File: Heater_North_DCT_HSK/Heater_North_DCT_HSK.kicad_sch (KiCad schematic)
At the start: 3 parts, among them J1 North_Heater_1, J2 North_Heater_2, J3 Internal_Heater_DCT_HSK_Box

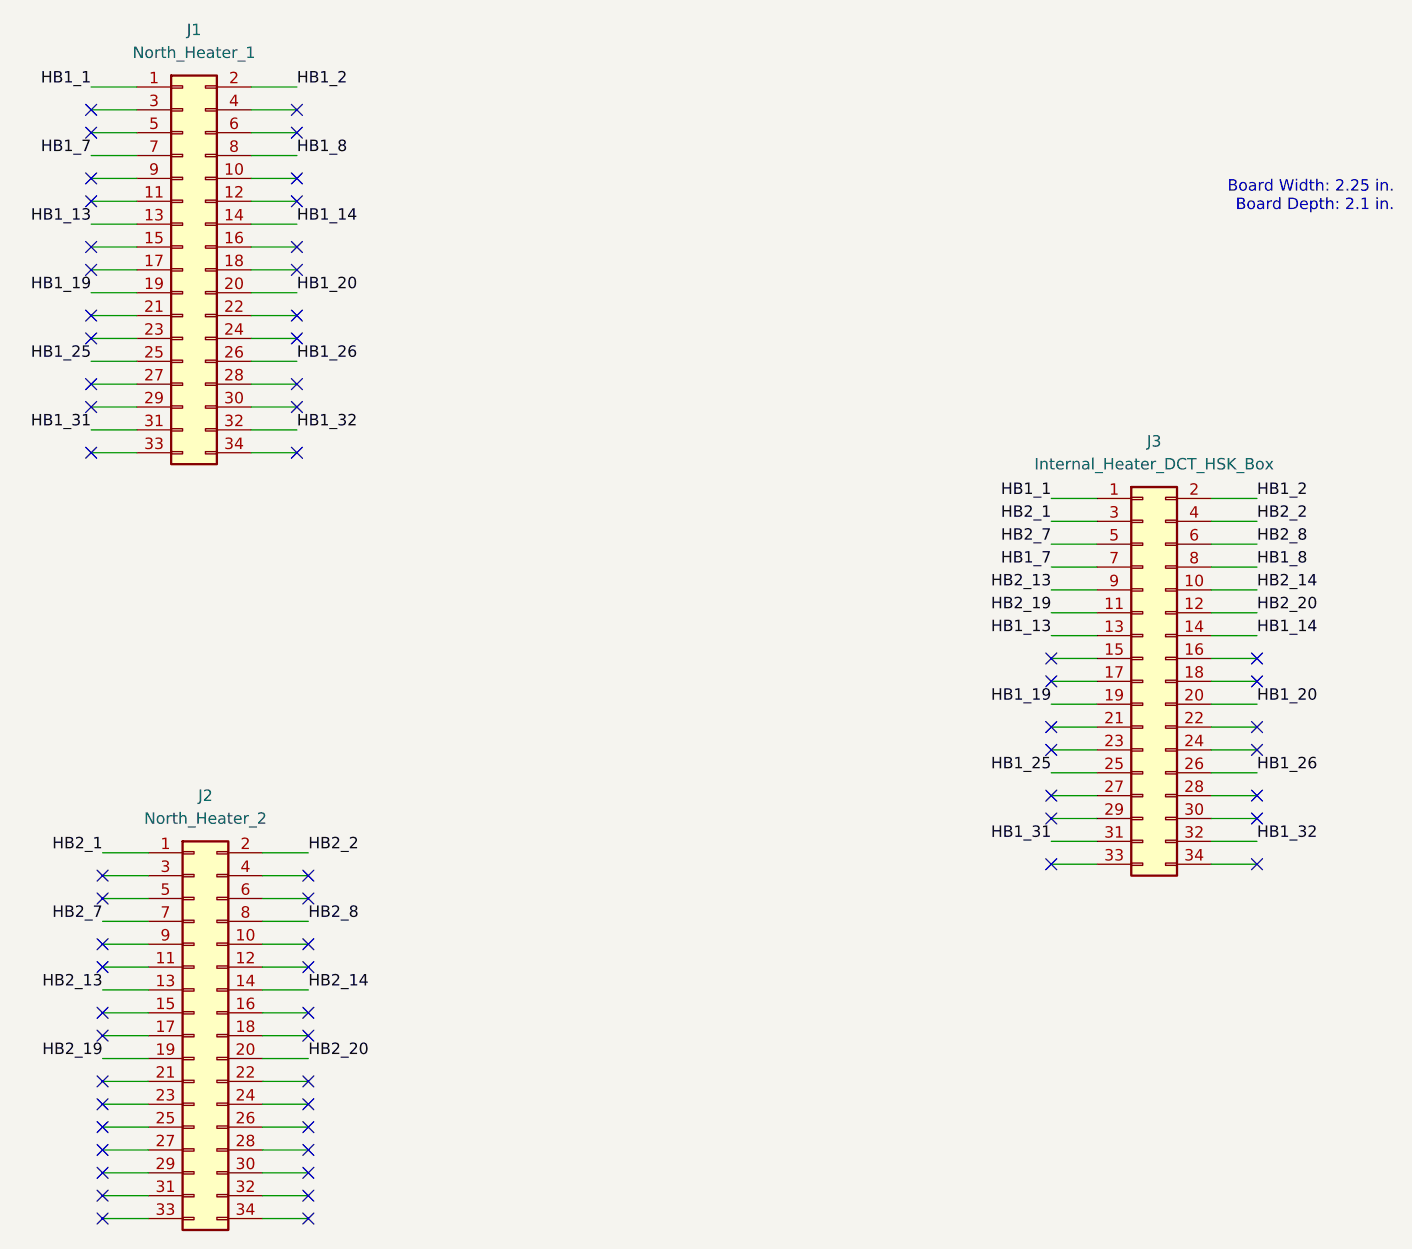
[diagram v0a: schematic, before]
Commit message: New feedthrough PCBs to access spare heater channels for flowcontroller heaters.
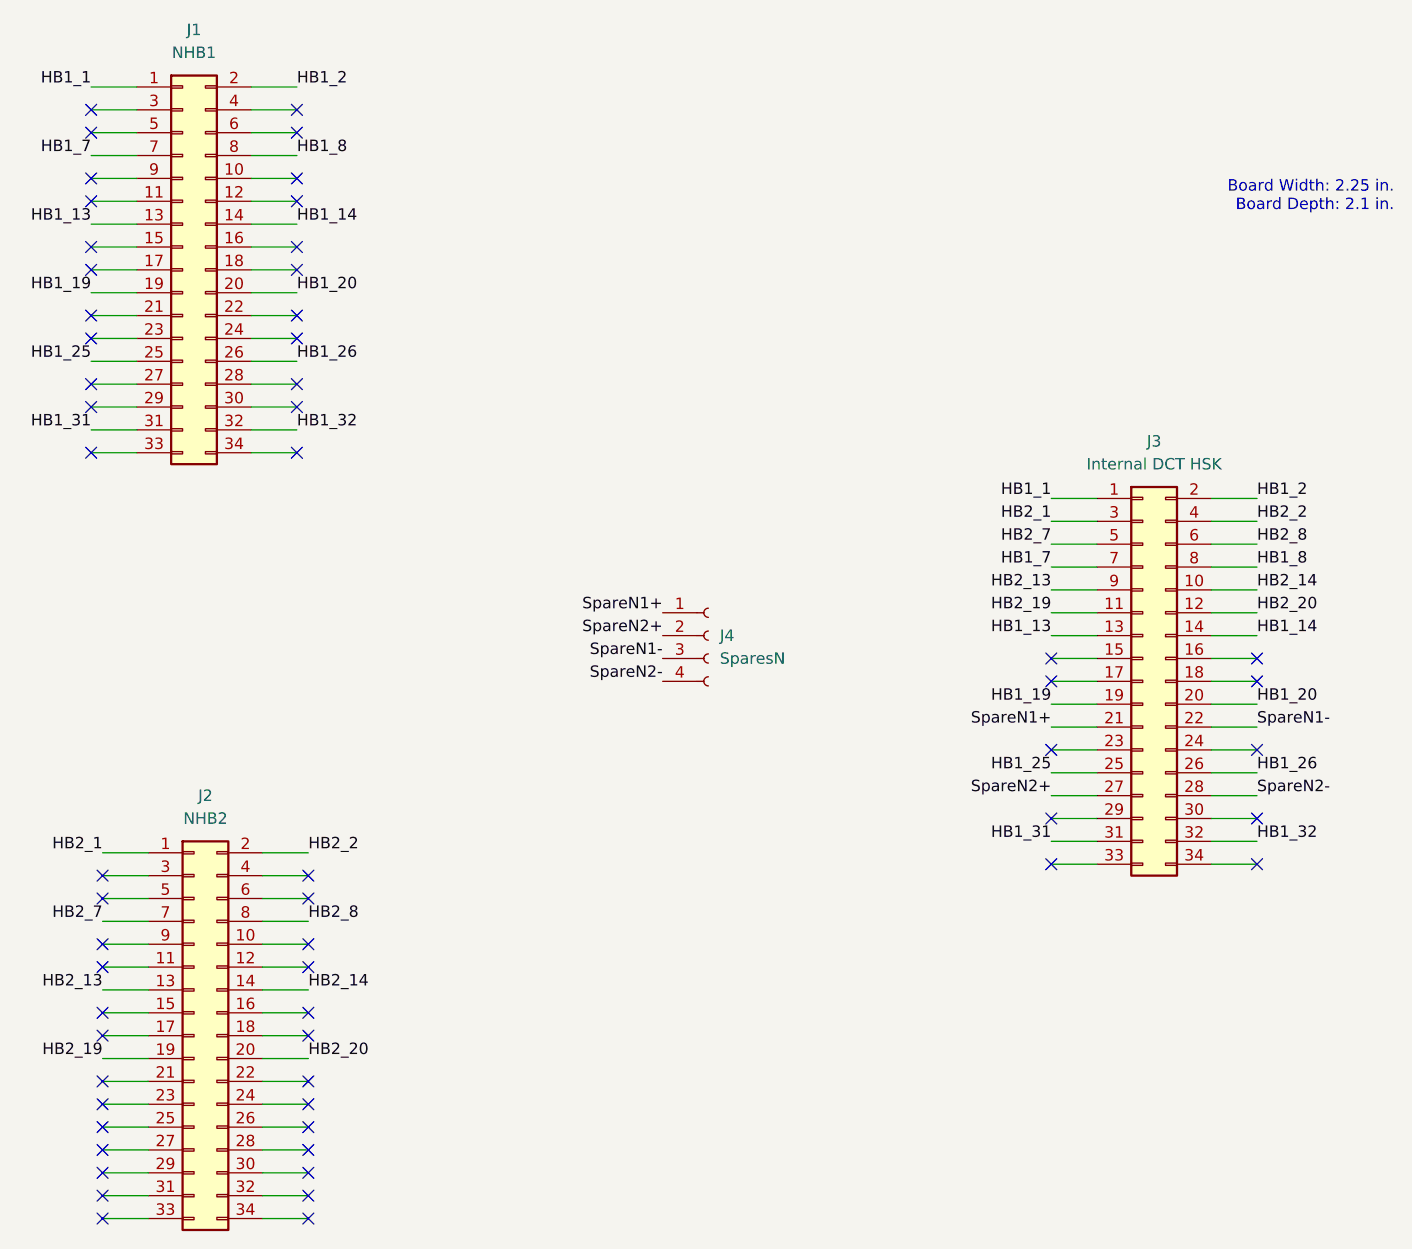
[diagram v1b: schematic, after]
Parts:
- added J4: SparesN, Connector_Molex:Molex_Micro-Fit_3.0_43045-0400_2x02_P3.00mm_Horizontal, symbol Connector:Conn_01x04_Socket
- J1: value North_Heater_1 -> NHB1
- J2: value North_Heater_2 -> NHB2
- J3: value Internal_Heater_DCT_HSK_Box -> Internal DCT HSK
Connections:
- net SpareN1+: now reaches J3.21 (Pin_21)
- net SpareN1+: now also J4.1 (Pin_1)
- net SpareN1-: now reaches J3.22 (Pin_22)
- net SpareN1-: now also J4.3 (Pin_3)
- net SpareN2+: now reaches J3.27 (Pin_27)
- net SpareN2+: now also J4.2 (Pin_2)
- net SpareN2-: now reaches J3.28 (Pin_28)
- net SpareN2-: now also J4.4 (Pin_4)
- no-connect marks 62 -> 58
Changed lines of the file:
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@@
   (no_connect (at 101.6 74.93))
   (no_connect (at 78.74 82.55))
-  (no_connect (at 208.28 120.65))
   (no_connect (at 185.42 123.19))
   (no_connect (at 78.74 62.23))
@@
   (no_connect (at 208.28 123.19))
   (no_connect (at 101.6 62.23))
-  (no_connect (at 208.28 113.03))
   (no_connect (at 101.6 59.69))
   (no_connect (at 102.87 167.64))
@@
   (no_connect (at 208.28 105.41))
   (no_connect (at 101.6 67.31))
-  (no_connect (at 185.42 120.65))
   (no_connect (at 78.74 59.69))
   (no_connect (at 101.6 69.85))
   (no_connect (at 78.74 74.93))
-  (no_connect (at 185.42 113.03))
   (no_connect (at 185.42 128.27))
   (no_connect (at 208.28 115.57))
@@
     (effects (font (size 1.27 1.27)) (justify left bottom))
   )
+  (label "SpareN1+" (at 142.24 100.33 180) (fields_autoplaced)
+    (effects (font (size 1.27 1.27)) (justify right bottom))
+  )
   (label "HB1_19" (at 185.42 110.49 180) (fields_autoplaced)
     (effects (font (size 1.27 1.27)) (justify right bottom))
   )
+  (label "SpareN2-" (at 142.24 107.95 180) (fields_autoplaced)
+    (effects (font (size 1.27 1.27)) (justify right bottom))
+  )
+  (label "SpareN2+" (at 142.24 102.87 180) (fields_autoplaced)
+    (effects (font (size 1.27 1.27)) (justify right bottom))
+  )
   (label "HB1_19" (at 78.74 64.77 180) (fields_autoplaced)
     (effects (font (size 1.27 1.27)) (justify right bottom))
@@
     (effects (font (size 1.27 1.27)) (justify left bottom))
   )
+  (label "SpareN1+" (at 185.42 113.03 180) (fields_autoplaced)
+    (effects (font (size 1.27 1.27)) (justify right bottom))
+  )
+  (label "SpareN2+" (at 185.42 120.65 180) (fields_autoplaced)
+    (effects (font (size 1.27 1.27)) (justify right bottom))
+  )
+  (label "SpareN2-" (at 208.28 120.65 0) (fields_autoplaced)
+    (effects (font (size 1.27 1.27)) (justify left bottom))
+  )
   (label "HB2_2" (at 102.87 127 0) (fields_autoplaced)
     (effects (font (size 1.27 1.27)) (justify left bottom))
@@
     (effects (font (size 1.27 1.27)) (justify left bottom))
   )
+  (label "SpareN1-" (at 208.28 113.03 0) (fields_autoplaced)
+    (effects (font (size 1.27 1.27)) (justify left bottom))
+  )
   (label "HB2_14" (at 208.28 97.79 0) (fields_autoplaced)
     (effects (font (size 1.27 1.27)) (justify left bottom))
@@
   (label "HB1_8" (at 101.6 49.53 0) (fields_autoplaced)
     (effects (font (size 1.27 1.27)) (justify left bottom))
+  )
+  (label "SpareN1-" (at 142.24 105.41 180) (fields_autoplaced)
+    (effects (font (size 1.27 1.27)) (justify right bottom))
   )
   (label "HB2_8" (at 208.28 92.71 0) (fields_autoplaced)
@@
       (effects (font (size 1.27 1.27)))
     )
-    (property "Value" "Internal_Heater_DCT_HSK_Box" (at 196.85 83.82 0)
+    (property "Value" "Internal DCT HSK" (at 196.85 83.82 0)
       (effects (font (size 1.27 1.27)))
     )
@@
     )
   )
+  (symbol (lib_id "Connector:Conn_01x04_Socket") (at 147.32 102.87 0) (unit 1)
+    (in_bom yes) (on_board yes) (dnp no) (fields_autoplaced)
+    (property "Reference" "J4" (at 148.59 102.87 0)
+      (effects (font (size 1.27 1.27)) (justify left))
+    )
+    (property "Value" "SparesN" (at 148.59 105.41 0)
+      (effects (font (size 1.27 1.27)) (justify left))
+    )
+    (property "Footprint" "Connector_Molex:Molex_Micro-Fit_3.0_43045-0400_2x02_P3.00mm_Horizontal" (at 147.32 102.87 0)
+      (effects (font (size 1.27 1.27)) hide)
+    )
+    (property "Datasheet" "~" (at 147.32 102.87 0)
+      (effects (font (size 1.27 1.27)) hide)
+    )
+    (pin "1")
+    (pin "2")
+    (pin "3")
+    (pin "4")
+    (instances
+      (project "Heater_North_DCT_HSK"
+        (path "/b67bdb50-32e2-49f2-b2ed-35caa82406e6"
+          (reference "J4") (unit 1)
+        )
+      )
+    )
+  )
   (symbol (lib_id "Connector_Generic:Conn_02x17_Odd_Even") (at 88.9 62.23 0) (unit 1)
     (in_bom yes) (on_board yes) (dnp no) (fields_autoplaced)
@@
       (effects (font (size 1.27 1.27)))
     )
-    (property "Value" "North_Heater_1" (at 90.17 38.1 0)
+    (property "Value" "NHB1" (at 90.17 38.1 0)
       (effects (font (size 1.27 1.27)))
     )
@@
       (effects (font (size 1.27 1.27)))
     )
-    (property "Value" "North_Heater_2" (at 91.44 123.19 0)
+    (property "Value" "NHB2" (at 91.44 123.19 0)
       (effects (font (size 1.27 1.27)))
     )
